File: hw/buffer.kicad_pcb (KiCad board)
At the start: 4 copper layers, 31 parts, among them J10 RFShield_Back, J6 RFShield_Front, K1 G6L-1F, U10 AQY280S, U11 TS5A63157DCK, U12 OPA859xDSG, U13 AD8370

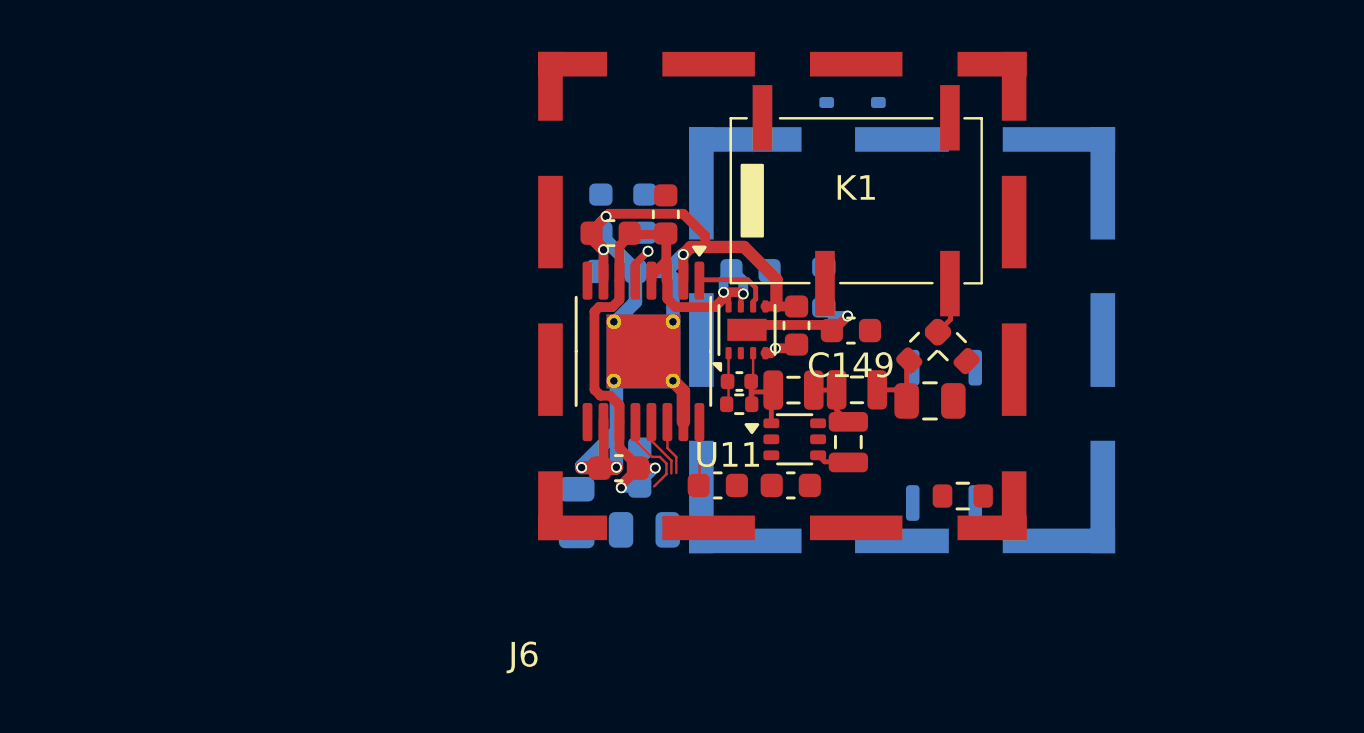
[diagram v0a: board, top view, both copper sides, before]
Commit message: split buffer into sub-pcb buffer.kicad.pcb
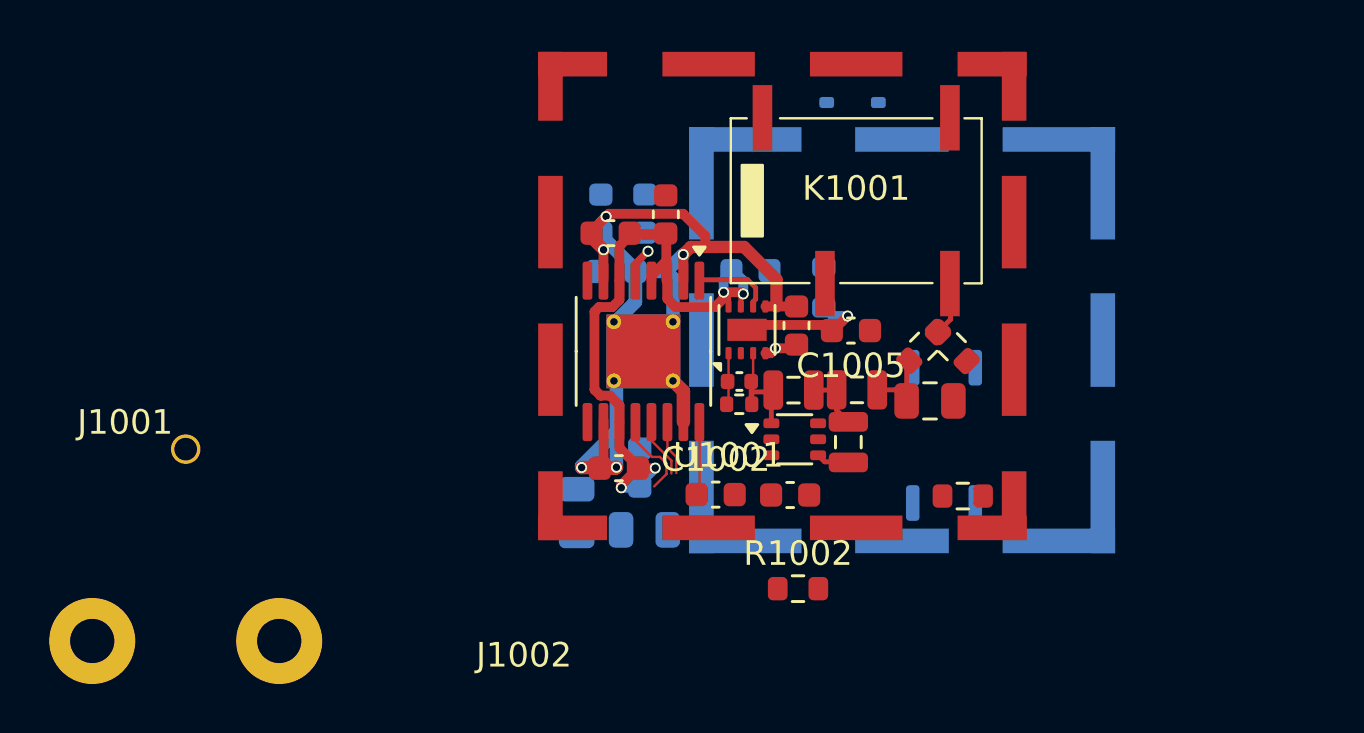
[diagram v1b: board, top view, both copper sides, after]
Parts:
- removed C111: 100n, Capacitor_SMD:C_0603_1608Metric
- added C1002: 100n, Capacitor_SMD:C_0603_1608Metric, F.Cu at (183.3, 87.0)
- added J1001: BNC, proj_footprints:BNC_Molex_0731713150, F.Cu at (161.7, 92.9)
- added R1002: 100k, Resistor_SMD:R_0603_1608Metric, F.Cu at (186.6, 90.8)
- moved C1001 0.39 mm to (186.3, 87.0)
- renumbered C70 to C1001, C20 to C1003, C66 to C1004, C149 to C1005, C76 to C1006, C9 to C1007, C67 to C1008, C68 to C1009, C69 to C1010, C71 to C1011, C73 to C1012, C74 to C1013, C75 to C1014, C23 to C1015, C26 to C1016, D7 to D1001, J6 to J1002, J10 to J1003, JP4 to JP1001, K1 to K1001, R42 to R1001, R17 to R1003, R50 to R1004, R48 to R1005, R49 to R1006, R127 to R1007, U11 to U1001, U10 to U1002, U13 to U1003, U12 to U1004
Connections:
- net /ADC/ADC_CHA_IN_N renamed /OUTN
- net /ADC/ADC_CHA_IN_P renamed /OUTP
- net /Front End/FE_CHA/FE_CTL_AC renamed /FE_CTL_AC
- net /Front End/FE_CHA/FE_CTL_TERM renamed /FE_CTL_TERM
- net /Front End/FE_CHA/PGA_CTL_CLK renamed /PGA_CTL_CLK
- net /Front End/FE_CHA/PGA_CTL_DATA renamed /PGA_CTL_DATA
- net /Front End/FE_CHA/PGA_CTL_LATCH renamed /PGA_CTL_LATCH
- net /Front End/FE_CHA/PGA_INHI renamed Net-(U1003-INHI)
- C1005 pad 1: GND -> GNDA
- C1006 pad 2: GND -> GNDA
- C1007 pad 2: GND -> GNDA
- C1008 pad 2: GND -> GNDA
- C1009 pad 2: GND -> GNDA
- C1010 pad 2: GND -> GNDA
- C1011 pad 2: GND -> GNDA
- C1012 pad 2: GND -> GNDA
- C1013 pad 2: GND -> GNDA
- C1014 pad 2: GND -> GNDA
- J1002 pad 1: GND -> GNDA
- J1003 pad 1: GND -> GNDA
- K1001 pad 2: GND -> GNDA
- U1001 pad 3: GND -> GNDA
- U1001 pad 6: /Front End/FE_CHA/FE_CTL_ATT -> /FE_CTL_ATT
- U1003 pad 16: /Front End/FE_CHA/PGA_INLO -> /PGA_INLO
- U1004 pad 4: GND -> GNDA
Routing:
- net /PGA_INLO: track 0.00 -> 2.64 mm
- net /Front End/FE_CHA/PGA_INLO: track 2.64 -> 0.00 mm
- net GNDA: track 0.00 -> 1.44 mm, vias 0 -> 1
- net GND: track 1.44 -> 0.00 mm, vias 1 -> 0

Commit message: buffer layout almost complete, PGA in through two cage gaps
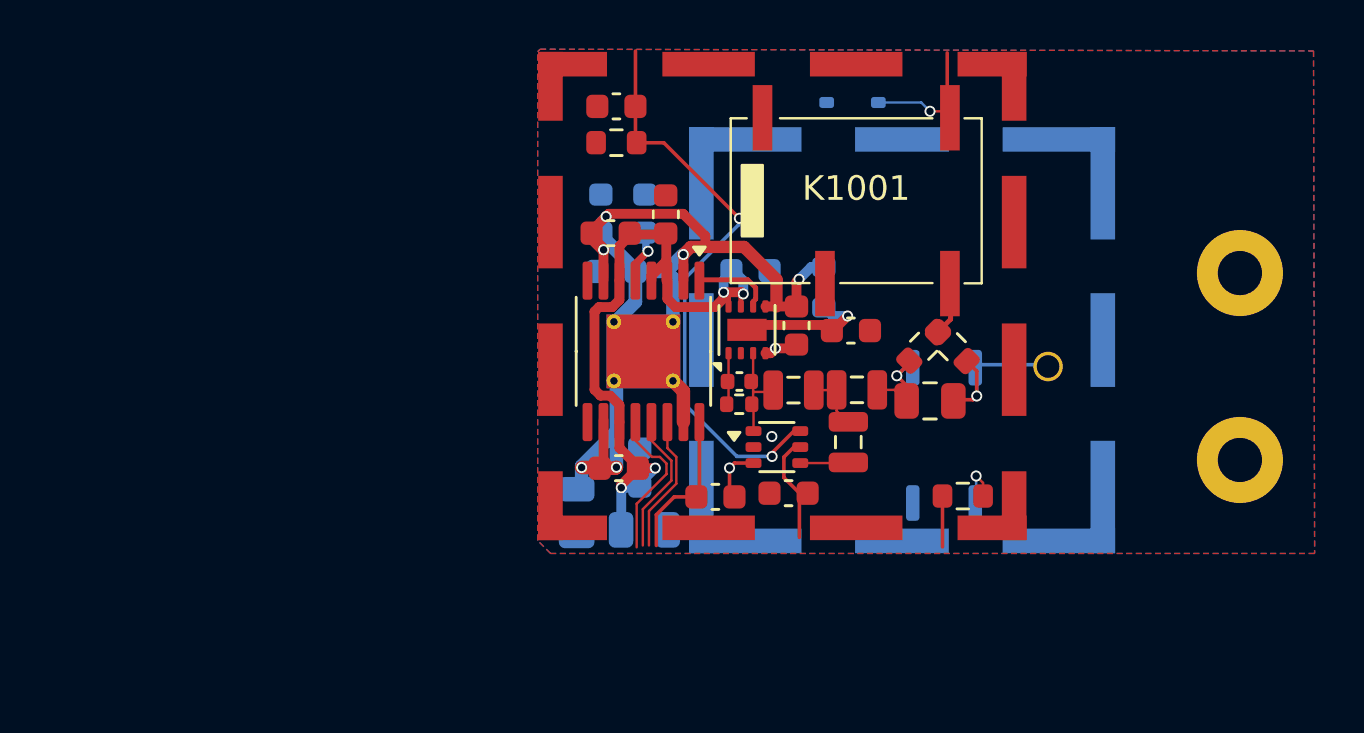
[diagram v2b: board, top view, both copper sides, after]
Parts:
- added C1001: 100n, Capacitor_SMD:C_0603_1608Metric, F.Cu at (179.2, 71.2)
- R1002: value 100k -> 1M
- moved J1001 44.3 mm to (204.6, 81.8), turned to 90 degrees
- moved R1002 19.6 mm to (179.2, 72.7)
- moved U1001 0.79 mm to (185.8, 85.0)
- moved C1002 0.10 mm to (186.2, 86.9)
- moved C1003 0.09 mm to (183.3, 87.1)
- renumbered C1001 to C1002, C1002 to C1003, C1003 to C1004, C1004 to C1005, C1005 to C1006, C1006 to C1007, C1007 to C1008, C1008 to C1009, C1009 to C1010, C1010 to C1011, C1011 to C1012, C1012 to C1013, C1013 to C1014, C1014 to C1015, C1015 to C1016, C1016 to C1017
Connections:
- C1003 pad 2: GNDA -> GND
- C1006 pad 1: GNDA -> GND
- C1007 pad 2: GNDA -> GND
- C1008 pad 2: GNDA -> GND
- C1009 pad 2: GNDA -> GND
- C1010 pad 2: GNDA -> GND
- C1011 pad 2: GNDA -> GND
- C1012 pad 2: GNDA -> GND
- C1013 pad 2: GNDA -> GND
- C1014 pad 2: GNDA -> GND
- C1015 pad 2: GNDA -> GND
- J1001 pad 2: GNDA -> GND
- J1002 pad 1: GNDA -> GND
- J1003 pad 1: GNDA -> GND
- K1001 pad 2: GNDA -> GND
- U1001 pad 3: GNDA -> GND
- U1004 pad 4: GNDA -> GND
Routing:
- net /FE_CTL_ATT: track 0.00 -> 23.9 mm, vias 0 -> 2
- net Net-(J1001-In): track 0.00 -> 6.73 mm, vias 0 -> 1
- net /FE_CTL_TERM: track 0.00 -> 5.76 mm, vias 0 -> 1
- net Vpp_analog: track 0.00 -> 4.81 mm
- net GND: track 0.00 -> 3.78 mm, vias 0 -> 3
- net /PGA_INLO: track 2.64 -> 6.24 mm
- net -2V5_analog: track 37.5 -> 41.0 mm, vias 5 -> 6
- net /PGA_CTL_CLK: track 2.42 -> 5.83 mm
- net /PGA_CTL_DATA: track 2.22 -> 5.63 mm
- net /PGA_CTL_LATCH: track 3.53 -> 6.30 mm
- net /FE_CTL_AC: track 0.00 -> 2.07 mm
- net Net-(R1001-Pad1): track 0.00 -> 2.02 mm, vias 0 -> 1
- net +2V5_analog: track 27.0 -> 28.8 mm
- net GNDA: track 1.44 -> 0.00 mm, vias 1 -> 0
- net Net-(JP1001-B): track 3.09 -> 4.41 mm, vias 0 -> 1
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- added copper zone on B.Cu, net GND
- added copper zone on F.Cu, net GND
- added copper zone on In1.Cu, net GND
- added copper zone on In2.Cu, net GND

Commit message: buffer edited; ready for merge CHA
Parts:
- added R1001: 1M, Resistor_SMD:R_0603_1608Metric, F.Cu at (181.2, 72.0)
- moved C1001 2.19 mm to (179.0, 73.4)
- moved J1001 2.00 mm to (204.6, 83.8)
- moved R1003 1.12 mm to (179.0, 71.6)
- moved R1002 0.57 mm to (192.9, 86.6)
- renumbered R1001 to R1002, R1002 to R1003, R1003 to R1004, R1004 to R1005, R1005 to R1006, R1006 to R1007, R1007 to R1008
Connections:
- C1001 pad 1: /FE_CTL_ATT -> Net-(U1001-IN)
- U1001 pad 6: /FE_CTL_ATT -> Net-(U1001-IN)
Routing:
- net Net-(U1001-IN): track 0.00 -> 20.8 mm, vias 0 -> 2
- net /FE_CTL_ATT: track 23.9 -> 3.78 mm, vias 2 -> 0
- net -2V5_analog: track 41.0 -> 42.1 mm, vias 6 -> 7
- net Net-(J1001-In): track 6.73 -> 7.56 mm
- net GND: vias 3 -> 31

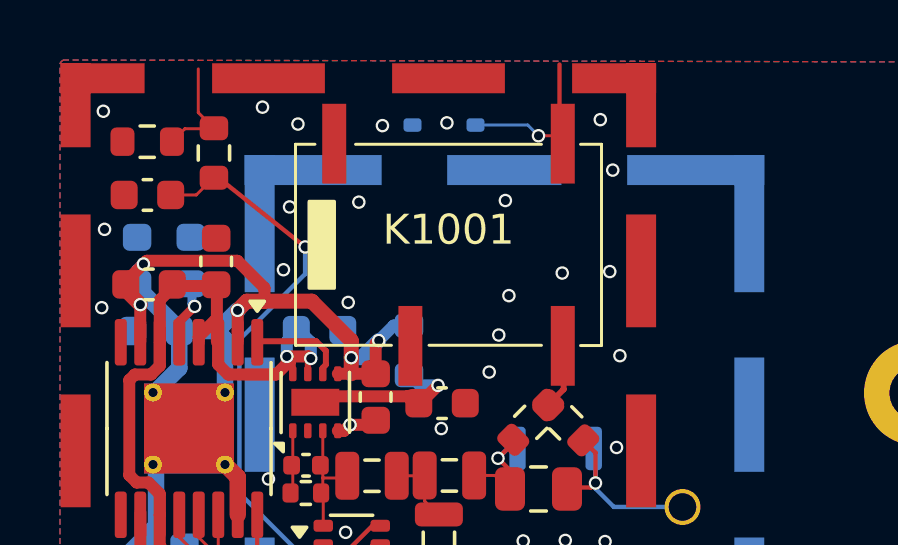
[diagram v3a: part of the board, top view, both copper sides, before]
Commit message: buffer: reannotated and updated pcb for FE_CHB
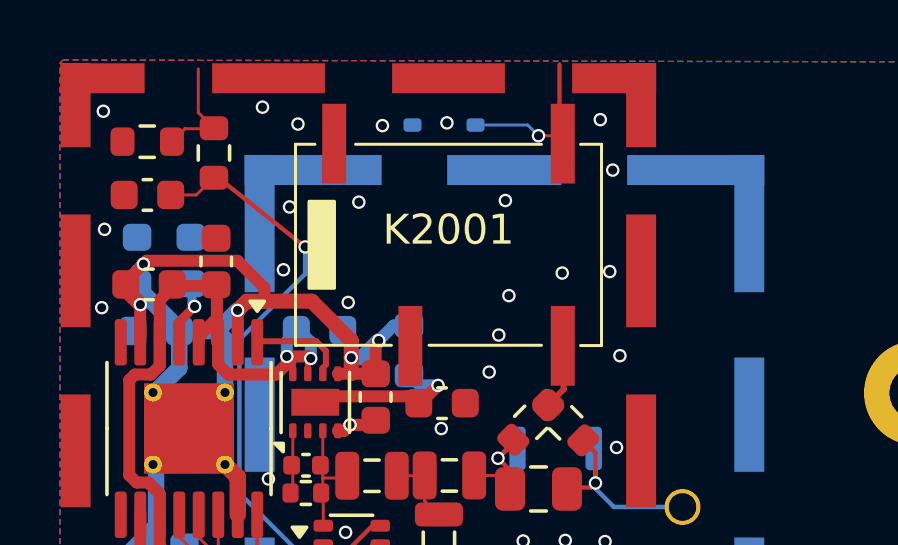
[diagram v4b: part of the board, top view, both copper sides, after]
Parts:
- renumbered C1001 to C2001, C1002 to C2002, C1003 to C2003, C1004 to C2004, C1005 to C2005, C1006 to C2006, C1007 to C2007, C1008 to C2008, C1009 to C2009, C1010 to C2010, C1011 to C2011, C1012 to C2012, C1013 to C2013, C1014 to C2014, C1015 to C2015, C1016 to C2016, C1017 to C2017, D1001 to D2001, J1001 to J2001, J1002 to J2002, J1003 to J2003, JP1001 to JP2001, K1001 to K2001, R1001 to R2001, R1002 to R2002, R1003 to R2003, R1004 to R2004, R1005 to R2005, R1006 to R2006, R1007 to R2007, R1008 to R2008, U1001 to U2001, U1002 to U2002, U1003 to U2003, U1004 to U2004
